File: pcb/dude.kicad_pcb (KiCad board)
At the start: 2 copper layers, 34.7 x 16.8 mm, 14 parts, among them CON1 AVR-ISP-6, CON2 USB-MINI-B, IC1 ATTINY85-P, P1 CONN_5

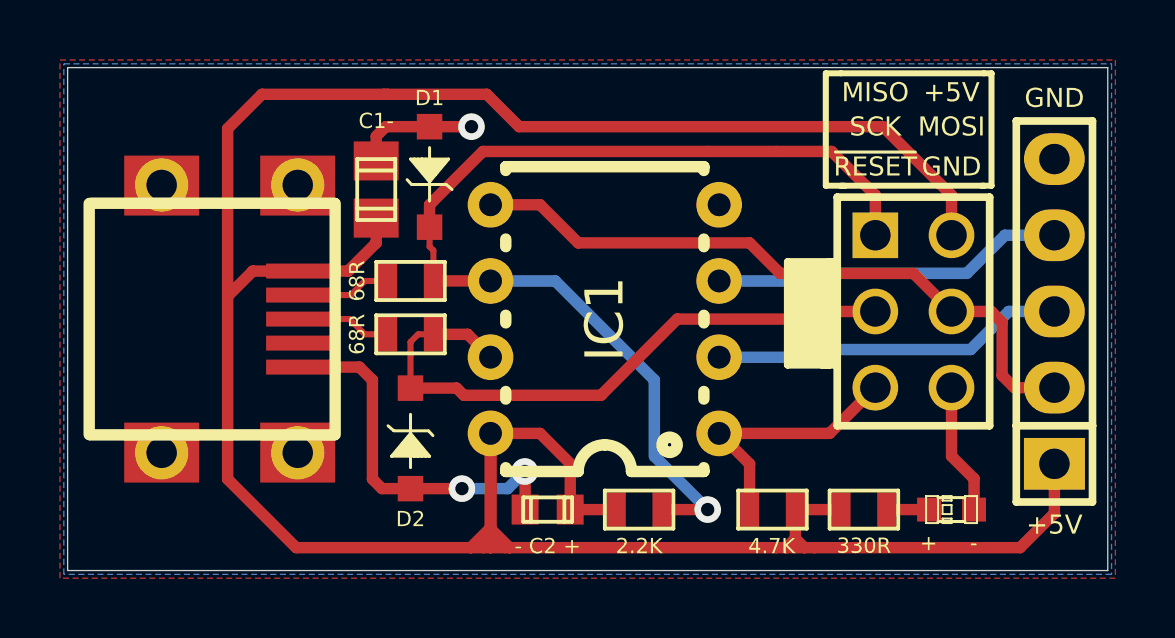
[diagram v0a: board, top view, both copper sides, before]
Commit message: Update silkscreen
- Switched naming to "1209: Fade" to reflect VID/PID
- A placement label for the optional power LED is now present
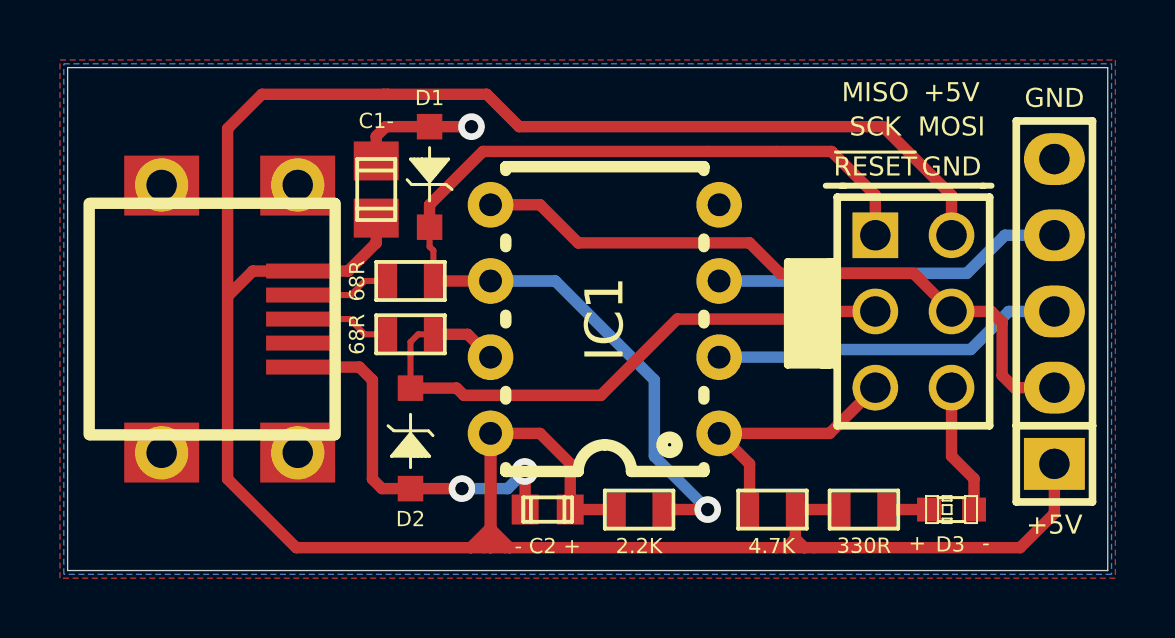
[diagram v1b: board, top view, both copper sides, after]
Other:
- board text added: "1209: Fade 2017-05-05"
- board text added: "D3"
- board text removed: "dude 2015-05-31"
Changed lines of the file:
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@@
-(kicad_pcb (version 3) (host pcbnew "(2014-jan-25)-product")
+(kicad_pcb (version 4) (host pcbnew 4.0.6)
   (general
     (links 32)
@@
     (area 96.761299 86.093299 131.457701 102.882701)
     (thickness 1.6002)
-    (drawings 30)
+    (drawings 26)
     (tracks 122)
     (zones 0)
@@
   (page A4)
   (layers
-    (15 Front signal)
-    (0 Back signal)
-    (17 F.Adhes user)
-    (19 F.Paste user)
-    (20 B.SilkS user)
-    (21 F.SilkS user)
-    (22 B.Mask user)
-    (23 F.Mask user)
-    (28 Edge.Cuts user)
+    (0 Front signal)
+    (31 Back signal)
+    (33 F.Adhes user)
+    (35 F.Paste user)
+    (36 B.SilkS user)
+    (37 F.SilkS user)
+    (38 B.Mask user)
+    (39 F.Mask user)
+    (44 Edge.Cuts user)
   )
   (setup
@@
     (visible_elements 7FFFFF7F)
     (pcbplotparams
-      (layerselection 284196865)
+      (layerselection 0x00030_80000001)
       (usegerberextensions true)
       (excludeedgelayer false)
@@
       (plotreference true)
       (plotvalue true)
-      (plotothertext true)
       (plotinvisibletext false)
       (padsonsilk false)
@@
     (uvia_drill 0.127)
   )
+  (module Pin_Headers:Pin_Header_Straight_1x05 (layer Front)
+    (at 129.667 94.234 90)
+    (descr "1 pin")
+    (tags "CONN DEV")
+    (fp_text reference P1 (at 0 -2.286 90) (layer F.SilkS) hide
+      (effects (font (size 1.27 1.27) (thickness 0.2032)))
+    )
+    (fp_text value CONN_5 (at 0 0 90) (layer F.SilkS) hide
+      (effects (font (size 1.27 1.27) (thickness 0.2032)))
+    )
+    (fp_line (start -3.81 -1.27) (end 6.35 -1.27) (layer F.SilkS) (width 0.254))
+    (fp_line (start 6.35 -1.27) (end 6.35 1.27) (layer F.SilkS) (width 0.254))
+    (fp_line (start 6.35 1.27) (end -3.81 1.27) (layer F.SilkS) (width 0.254))
+    (fp_line (start -6.35 -1.27) (end -3.81 -1.27) (layer F.SilkS) (width 0.254))
+    (fp_line (start -3.81 -1.27) (end -3.81 1.27) (layer F.SilkS) (width 0.254))
+    (fp_line (start -6.35 -1.27) (end -6.35 1.27) (layer F.SilkS) (width 0.254))
+    (fp_line (start -6.35 1.27) (end -3.81 1.27) (layer F.SilkS) (width 0.254))
+    (pad 1 thru_hole rect (at -5.08 0 90) (size 1.7272 2.032) (drill 1.016) (layers *.Cu *.Mask F.SilkS)
+      (net 1 +5V))
+    (pad 2 thru_hole oval (at -2.54 0 90) (size 1.7272 2.032) (drill 1.016) (layers *.Cu *.Mask F.SilkS)
+      (net 15 MOSI))
+    (pad 3 thru_hole oval (at 0 0 90) (size 1.7272 2.032) (drill 1.016) (layers *.Cu *.Mask F.SilkS)
+      (net 9 "Net-(IC1-Pad2)"))
+    (pad 4 thru_hole oval (at 2.54 0 90) (size 1.7272 2.032) (drill 1.016) (layers *.Cu *.Mask F.SilkS)
+      (net 8 "Net-(IC1-Pad3)"))
+    (pad 5 thru_hole oval (at 5.08 0 90) (size 1.7272 2.032) (drill 1.016) (layers *.Cu *.Mask F.SilkS)
+      (net 2 GND))
+    (model Pin_Headers/Pin_Header_Straight_1x05.wrl
+      (at (xyz 0 0 0))
+      (scale (xyz 1 1 1))
+      (rotate (xyz 0 0 0))
+    )
+  )
   (module SM0603 (layer Front)
     (at 120.269 100.838)
@@
     )
   )
-  (module Pin_Headers:Pin_Header_Straight_1x05 (layer Front)
-    (at 129.667 94.234 90)
-    (descr "1 pin")
-    (tags "CONN DEV")
-    (fp_text reference P1 (at 0 -2.286 90) (layer F.SilkS) hide
-      (effects (font (size 1.27 1.27) (thickness 0.2032)))
-    )
-    (fp_text value CONN_5 (at 0 0 90) (layer F.SilkS) hide
-      (effects (font (size 1.27 1.27) (thickness 0.2032)))
-    )
-    (fp_line (start -3.81 -1.27) (end 6.35 -1.27) (layer F.SilkS) (width 0.254))
-    (fp_line (start 6.35 -1.27) (end 6.35 1.27) (layer F.SilkS) (width 0.254))
-    (fp_line (start 6.35 1.27) (end -3.81 1.27) (layer F.SilkS) (width 0.254))
-    (fp_line (start -6.35 -1.27) (end -3.81 -1.27) (layer F.SilkS) (width 0.254))
-    (fp_line (start -3.81 -1.27) (end -3.81 1.27) (layer F.SilkS) (width 0.254))
-    (fp_line (start -6.35 -1.27) (end -6.35 1.27) (layer F.SilkS) (width 0.254))
-    (fp_line (start -6.35 1.27) (end -3.81 1.27) (layer F.SilkS) (width 0.254))
-    (pad 1 thru_hole rect (at -5.08 0 90) (size 1.7272 2.032) (drill 1.016) (layers *.Cu *.Mask F.SilkS)
-      (net 1 +5V))
-    (pad 2 thru_hole oval (at -2.54 0 90) (size 1.7272 2.032) (drill 1.016) (layers *.Cu *.Mask F.SilkS)
-      (net 15 MOSI))
-    (pad 3 thru_hole oval (at 0 0 90) (size 1.7272 2.032) (drill 1.016) (layers *.Cu *.Mask F.SilkS)
-      (net 9 "Net-(IC1-Pad2)"))
-    (pad 4 thru_hole oval (at 2.54 0 90) (size 1.7272 2.032) (drill 1.016) (layers *.Cu *.Mask F.SilkS)
-      (net 8 "Net-(IC1-Pad3)"))
-    (pad 5 thru_hole oval (at 5.08 0 90) (size 1.7272 2.032) (drill 1.016) (layers *.Cu *.Mask F.SilkS)
-      (net 2 GND))
-    (model Pin_Headers/Pin_Header_Straight_1x05.wrl
-      (at (xyz 0 0 0))
-      (scale (xyz 1 1 1))
-      (rotate (xyz 0 0 0))
-    )
-  )
   (module Capacitors_SMD:c_0805 (layer Front)
     (at 107.061 90.17 270)
@@
     (pad 14 thru_hole circle (at 3.3528 4.4577) (size 1.778 1.778) (drill 1.016) (layers *.Cu *.Mask F.SilkS))
   )
+  (gr_text D3 (at 126.2 102) (layer F.SilkS)
+    (effects (font (size 0.508 0.508) (thickness 0.1143)))
+  )
   (gr_line (start 127.5715 90.043) (end 127.254 90.043) (angle 90) (layer F.SilkS) (width 0.2))
-  (gr_line (start 127.5715 86.2965) (end 127.5715 90.043) (angle 90) (layer F.SilkS) (width 0.2))
-  (gr_line (start 127.3175 86.2965) (end 127.5715 86.2965) (angle 90) (layer F.SilkS) (width 0.2))
   (gr_line (start 122.047 90.043) (end 122.682 90.043) (angle 90) (layer F.SilkS) (width 0.2))
-  (gr_line (start 122.047 86.2965) (end 122.047 90.043) (angle 90) (layer F.SilkS) (width 0.2))
-  (gr_line (start 122.555 86.2965) (end 122.047 86.2965) (angle 90) (layer F.SilkS) (width 0.2))
-  (gr_line (start 127.3175 86.2965) (end 122.555 86.2965) (angle 90) (layer F.SilkS) (width 0.2))
   (gr_line (start 122.555 90.043) (end 127.3175 90.043) (angle 90) (layer F.SilkS) (width 0.2))
   (gr_text +5V (at 129.667 101.346) (layer F.SilkS)
@@
     (effects (font (size 0.508 0.508) (thickness 0.1143)))
   )
-  (gr_text - (at 126.9746 101.9556) (layer F.SilkS)
-    (effects (font (size 0.508 0.508) (thickness 0.1143)))
-  )
-  (gr_text + (at 125.476 101.9556) (layer F.SilkS)
+  (gr_text - (at 127.381 101.9556) (layer F.SilkS)
+    (effects (font (size 0.508 0.508) (thickness 0.1143)))
+  )
+  (gr_text + (at 125.095 101.9556) (layer F.SilkS)
     (effects (font (size 0.508 0.508) (thickness 0.1143)))
   )
@@
   (gr_line (start 96.774 102.87) (end 131.445 102.87) (angle 90) (layer Edge.Cuts) (width 0.0254))
   (gr_line (start 131.445 86.106) (end 131.445 102.87) (angle 90) (layer Edge.Cuts) (width 0.0254))
-  (gr_text "dude\n2015-05-31" (at 114.173 94.488 90) (layer B.SilkS)
+  (gr_text "1209: Fade\n2017-05-05" (at 114.173 94.488 90) (layer B.SilkS)
     (effects (font (size 1.143 1.143) (thickness 0.20955)) (justify mirror))
   )

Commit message: Add more helpful silkscreen
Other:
- board text added: "1209: Fade 2017-05-05 Open Collector"
- board text added: "RST"
- board text removed: "1209: Fade 2017-05-05"
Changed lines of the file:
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@@
     (links 32)
     (no_connects 0)
-    (area 96.761299 86.093299 131.457701 102.882701)
+    (area 94.619282 85.781896 131.858005 103.161084)
     (thickness 1.6002)
-    (drawings 26)
+    (drawings 44)
     (tracks 122)
     (zones 0)
@@
   (page A4)
   (layers
-    (0 Front signal)
+    (0 Front signal hide)
     (31 Back signal)
     (33 F.Adhes user)
@@
     (pad 14 thru_hole circle (at 3.3528 4.4577) (size 1.778 1.778) (drill 1.016) (layers *.Cu *.Mask F.SilkS))
   )
+  (gr_line (start 128.143 94.234) (end 128.27 94.234) (angle 90) (layer B.SilkS) (width 0.2))
+  (gr_line (start 126.873 95.504) (end 128.143 94.234) (angle 90) (layer B.SilkS) (width 0.2))
+  (gr_line (start 126.746 95.504) (end 126.873 95.504) (angle 90) (layer B.SilkS) (width 0.2))
+  (gr_line (start 121.158 95.504) (end 126.746 95.504) (angle 90) (layer B.SilkS) (width 0.2))
+  (gr_line (start 120.904 95.758) (end 121.158 95.504) (angle 90) (layer B.SilkS) (width 0.2))
+  (gr_line (start 119.634 95.758) (end 120.904 95.758) (angle 90) (layer B.SilkS) (width 0.2))
+  (gr_line (start 128.016 91.694) (end 128.27 91.694) (angle 90) (layer B.SilkS) (width 0.2))
+  (gr_line (start 126.746 92.964) (end 128.016 91.694) (angle 90) (layer B.SilkS) (width 0.2))
+  (gr_line (start 126.619 92.964) (end 126.746 92.964) (angle 90) (layer B.SilkS) (width 0.2))
+  (gr_line (start 121.793 92.964) (end 126.619 92.964) (angle 90) (layer B.SilkS) (width 0.2))
+  (gr_line (start 121.539 93.218) (end 119.634 93.218) (angle 90) (layer B.SilkS) (width 0.2))
+  (gr_line (start 121.793 92.964) (end 121.539 93.218) (angle 90) (layer B.SilkS) (width 0.2))
+  (gr_text RST (at 121.031 98.298) (layer B.SilkS)
+    (effects (font (size 0.762 0.762) (thickness 0.127)) (justify mirror))
+  )
+  (gr_text GND (at 121.031 90.678) (layer B.SilkS)
+    (effects (font (size 0.762 0.762) (thickness 0.127)) (justify mirror))
+  )
+  (gr_text +5V (at 108.204 98.298) (layer B.SilkS)
+    (effects (font (size 0.762 0.762) (thickness 0.127)) (justify mirror))
+  )
+  (gr_text SCK (at 108.204 95.758) (layer B.SilkS)
+    (effects (font (size 0.762 0.762) (thickness 0.127)) (justify mirror))
+  )
+  (gr_text MISO (at 108.204 93.218) (layer B.SilkS)
+    (effects (font (size 0.762 0.762) (thickness 0.127)) (justify mirror))
+  )
+  (gr_text MOSI (at 108.204 90.678) (layer B.SilkS)
+    (effects (font (size 0.762 0.762) (thickness 0.127)) (justify mirror))
+  )
   (gr_text D3 (at 126.2 102) (layer F.SilkS)
     (effects (font (size 0.508 0.508) (thickness 0.1143)))
@@
   (gr_line (start 96.774 102.87) (end 131.445 102.87) (angle 90) (layer Edge.Cuts) (width 0.0254))
   (gr_line (start 131.445 86.106) (end 131.445 102.87) (angle 90) (layer Edge.Cuts) (width 0.0254))
-  (gr_text "1209: Fade\n2017-05-05" (at 114.173 94.488 90) (layer B.SilkS)
+  (gr_text "1209: Fade\n2017-05-05\nOpen Collector" (at 114.681 94.488 90) (layer B.SilkS)
     (effects (font (size 1.143 1.143) (thickness 0.20955)) (justify mirror))
   )
@@
     (connect_pads (clearance 0.508))
     (min_thickness 0.254)
-    (fill (arc_segments 32) (thermal_gap 0.508) (thermal_bridge_width 0.508) (smoothing fillet))
+    (fill yes (arc_segments 32) (thermal_gap 0.508) (thermal_bridge_width 0.508) (smoothing fillet))
     (polygon
       (pts
@@
     (connect_pads (clearance 0.508))
     (min_thickness 0.254)
-    (fill (arc_segments 16) (thermal_gap 0.508) (thermal_bridge_width 0.508))
+    (fill yes (arc_segments 16) (thermal_gap 0.508) (thermal_bridge_width 0.508))
     (polygon
       (pts
